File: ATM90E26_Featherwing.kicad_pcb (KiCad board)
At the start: 2 copper layers, 49.9 x 39.4 mm, 59 parts, among them J1 AudioJack3, J2 4P-SMD-2.0-90D, J3 4P-SMD-2.0-90D, J4 12V AC, Q1 8.192MHz, U1 ATM90E26, U2 CJT1117-5.0-SOT223

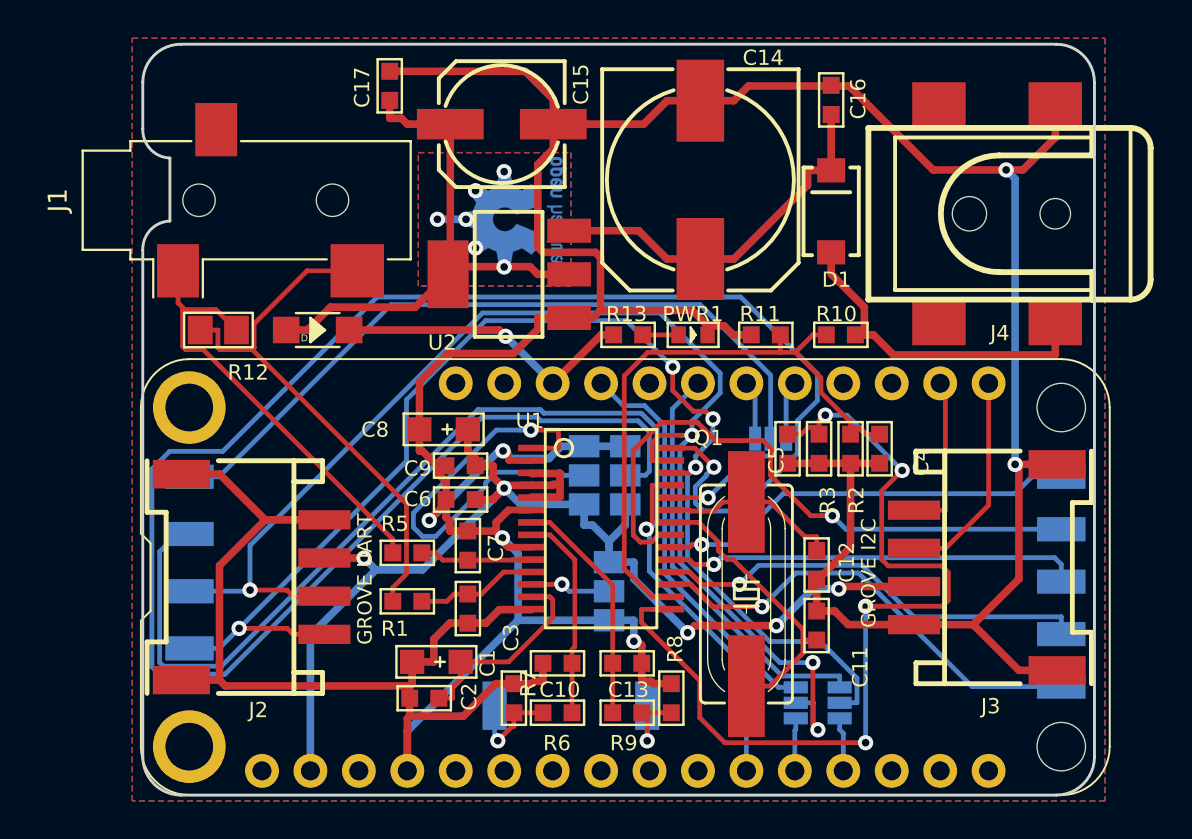
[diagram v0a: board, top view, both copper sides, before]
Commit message: Add stitchig vias
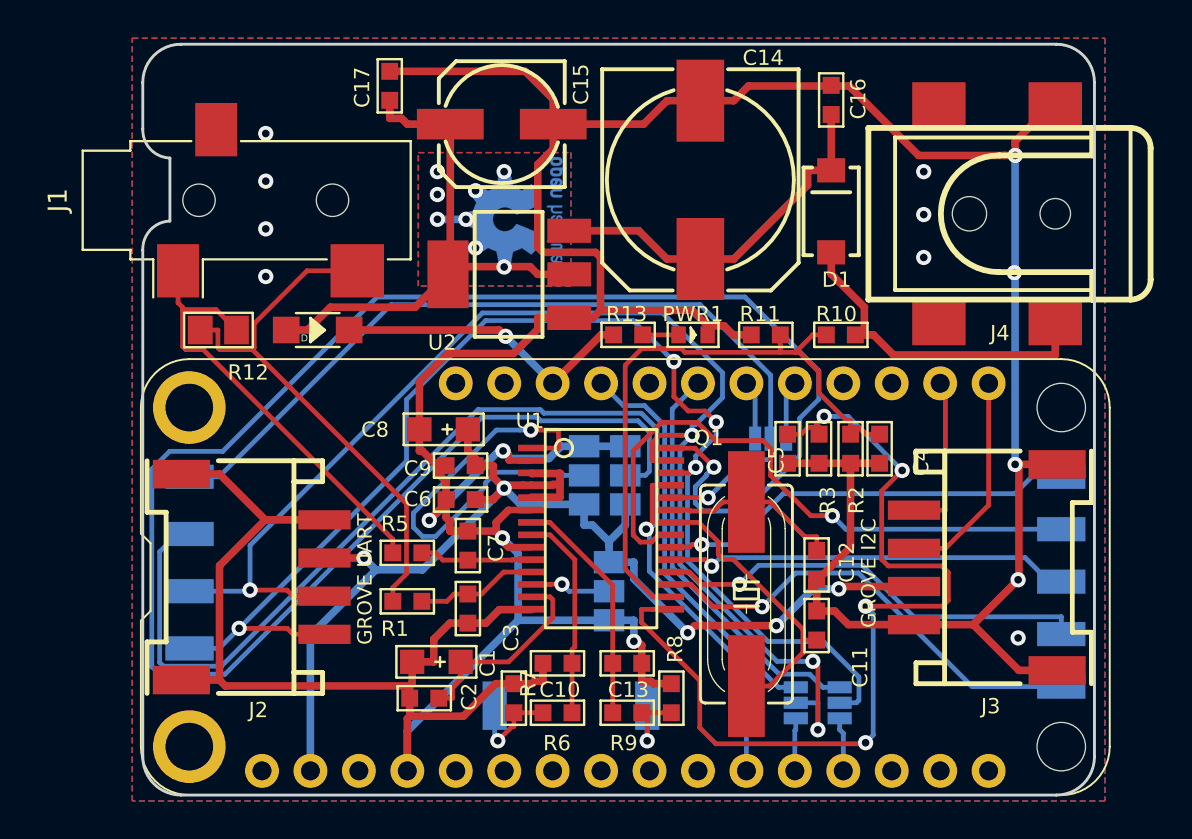
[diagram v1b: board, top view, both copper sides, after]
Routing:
- net /VN: track 47.9 -> 48.6 mm
- net /SO/TX: track 66.9 -> 67.6 mm
- net GND: track 240.4 -> 239.8 mm, vias 6 -> 16
- net /VP: track 32.8 -> 33.4 mm
- net /SI/RX: track 70.7 -> 71.3 mm
- net /5V_REG: vias 6 -> 8
